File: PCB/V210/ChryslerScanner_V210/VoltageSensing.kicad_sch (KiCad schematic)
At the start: 9 parts

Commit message: Completed schematic.
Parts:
- gave numbers to parts that had none: 9
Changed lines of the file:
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@@
   (symbol (lib_id "Device:R") (at 179.07 99.06 0) (unit 1)
     (in_bom yes) (on_board yes) (fields_autoplaced)
-    (property "Reference" "R?" (id 0) (at 181.61 97.7899 0)
+    (property "Reference" "R28" (id 0) (at 181.61 97.7899 0)
       (effects (font (size 1.27 1.27)) (justify left))
     )
@@
   (symbol (lib_id "power:+12V") (at 95.25 77.47 0) (unit 1)
     (in_bom yes) (on_board yes) (fields_autoplaced)
-    (property "Reference" "#PWR?" (id 0) (at 95.25 81.28 0)
+    (property "Reference" "#PWR035" (id 0) (at 95.25 81.28 0)
       (effects (font (size 1.27 1.27)) hide)
     )
@@
   (symbol (lib_id "Device:R") (at 95.25 99.06 0) (unit 1)
     (in_bom yes) (on_board yes) (fields_autoplaced)
-    (property "Reference" "R?" (id 0) (at 97.79 97.7899 0)
+    (property "Reference" "R24" (id 0) (at 97.79 97.7899 0)
       (effects (font (size 1.27 1.27)) (justify left))
     )
@@
   (symbol (lib_id "Device:R") (at 137.16 86.36 0) (unit 1)
     (in_bom yes) (on_board yes) (fields_autoplaced)
-    (property "Reference" "R?" (id 0) (at 139.7 85.0899 0)
+    (property "Reference" "R25" (id 0) (at 139.7 85.0899 0)
       (effects (font (size 1.27 1.27)) (justify left))
     )
@@
   (symbol (lib_id "power:VAA") (at 137.16 77.47 0) (unit 1)
     (in_bom yes) (on_board yes) (fields_autoplaced)
-    (property "Reference" "#PWR?" (id 0) (at 137.16 81.28 0)
+    (property "Reference" "#PWR037" (id 0) (at 137.16 81.28 0)
       (effects (font (size 1.27 1.27)) hide)
     )
@@
   (symbol (lib_id "Device:R") (at 179.07 86.36 0) (unit 1)
     (in_bom yes) (on_board yes) (fields_autoplaced)
-    (property "Reference" "R?" (id 0) (at 181.61 85.0899 0)
+    (property "Reference" "R27" (id 0) (at 181.61 85.0899 0)
       (effects (font (size 1.27 1.27)) (justify left))
     )
@@
   (symbol (lib_id "power:GND") (at 137.16 109.22 0) (unit 1)
     (in_bom yes) (on_board yes) (fields_autoplaced)
-    (property "Reference" "#PWR?" (id 0) (at 137.16 115.57 0)
+    (property "Reference" "#PWR038" (id 0) (at 137.16 115.57 0)
       (effects (font (size 1.27 1.27)) hide)
     )
@@
   (symbol (lib_id "Device:R") (at 95.25 86.36 0) (unit 1)
     (in_bom yes) (on_board yes) (fields_autoplaced)
-    (property "Reference" "R?" (id 0) (at 97.79 85.0899 0)
+    (property "Reference" "R23" (id 0) (at 97.79 85.0899 0)
       (effects (font (size 1.27 1.27)) (justify left))
     )
@@
   (symbol (lib_id "power:GND") (at 179.07 109.22 0) (unit 1)
     (in_bom yes) (on_board yes) (fields_autoplaced)
-    (property "Reference" "#PWR?" (id 0) (at 179.07 115.57 0)
+    (property "Reference" "#PWR040" (id 0) (at 179.07 115.57 0)
       (effects (font (size 1.27 1.27)) hide)
     )
@@
   (symbol (lib_id "Device:R") (at 137.16 99.06 0) (unit 1)
     (in_bom yes) (on_board yes) (fields_autoplaced)
-    (property "Reference" "R?" (id 0) (at 139.7 97.7899 0)
+    (property "Reference" "R26" (id 0) (at 139.7 97.7899 0)
       (effects (font (size 1.27 1.27)) (justify left))
     )
@@
   (symbol (lib_id "power:GND") (at 95.25 109.22 0) (unit 1)
     (in_bom yes) (on_board yes) (fields_autoplaced)
-    (property "Reference" "#PWR?" (id 0) (at 95.25 115.57 0)
+    (property "Reference" "#PWR036" (id 0) (at 95.25 115.57 0)
       (effects (font (size 1.27 1.27)) hide)
     )
@@
   (symbol (lib_id "Device:C") (at 107.95 99.06 0) (unit 1)
     (in_bom yes) (on_board yes) (fields_autoplaced)
-    (property "Reference" "C?" (id 0) (at 111.76 97.7899 0)
+    (property "Reference" "C16" (id 0) (at 111.76 97.7899 0)
       (effects (font (size 1.27 1.27)) (justify left))
     )
@@
   (symbol (lib_id "Device:C") (at 191.77 99.06 0) (unit 1)
     (in_bom yes) (on_board yes) (fields_autoplaced)
-    (property "Reference" "C?" (id 0) (at 195.58 97.7899 0)
+    (property "Reference" "C18" (id 0) (at 195.58 97.7899 0)
       (effects (font (size 1.27 1.27)) (justify left))
     )
@@
   (symbol (lib_id "power:VPP") (at 179.07 77.47 0) (unit 1)
     (in_bom yes) (on_board yes) (fields_autoplaced)
-    (property "Reference" "#PWR?" (id 0) (at 179.07 81.28 0)
+    (property "Reference" "#PWR039" (id 0) (at 179.07 81.28 0)
       (effects (font (size 1.27 1.27)) hide)
     )
@@
   (symbol (lib_id "Device:C") (at 149.86 99.06 0) (unit 1)
     (in_bom yes) (on_board yes) (fields_autoplaced)
-    (property "Reference" "C?" (id 0) (at 153.67 97.7899 0)
-      (effects (font (size 1.27 1.27)) (justify left))
-    )
+    (property "Reference" "C17" (id 0) (at 153.67 97.7899 0)
+      (effects (font (size 1.27 1.27)) (justify left))
+    )

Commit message: WIP
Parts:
- C16, C17, C18: footprint (none) -> Capacitor_SMD:C_0603_1608Metric
- R21: renamed from R23; footprint (none) -> Resistor_SMD:R_0603_1608Metric
- R22: renamed from R24; footprint (none) -> Resistor_SMD:R_0603_1608Metric
- R23: renamed from R25; footprint (none) -> Resistor_SMD:R_0603_1608Metric
- R24: renamed from R26; footprint (none) -> Resistor_SMD:R_0603_1608Metric
- R25: renamed from R27; footprint (none) -> Resistor_SMD:R_0603_1608Metric
- R26: renamed from R28; footprint (none) -> Resistor_SMD:R_0603_1608Metric
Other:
- title: Chrysler Scanner -> TJ Diag
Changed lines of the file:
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@@
   (paper "A4")
   (title_block
-    (title "Chrysler Scanner")
-    (date "2023-06-25")
-    (rev "V2.11")
+    (title "TJ Diag")
+    (date "2023-07-01")
+    (rev "V1.00")
     (company "andy@britishideas.com")
     (comment 1 "V210/ChryslerScanner_V210/schematic/ChryslerScanner_V210_schematic.pdf")
@@
   (symbol (lib_id "Device:R") (at 179.07 99.06 0) (unit 1)
     (in_bom yes) (on_board yes) (fields_autoplaced)
-    (property "Reference" "R28" (id 0) (at 181.61 97.7899 0)
+    (property "Reference" "R26" (id 0) (at 181.61 97.7899 0)
       (effects (font (size 1.27 1.27)) (justify left))
     )
@@
       (effects (font (size 1.27 1.27)) (justify left))
     )
-    (property "Footprint" "" (id 2) (at 177.292 99.06 90)
+    (property "Footprint" "Resistor_SMD:R_0603_1608Metric" (id 2) (at 177.292 99.06 90)
       (effects (font (size 1.27 1.27)) hide)
     )
@@
   (symbol (lib_id "power:+12V") (at 95.25 77.47 0) (unit 1)
     (in_bom yes) (on_board yes) (fields_autoplaced)
-    (property "Reference" "#PWR035" (id 0) (at 95.25 81.28 0)
+    (property "Reference" "#PWR031" (id 0) (at 95.25 81.28 0)
       (effects (font (size 1.27 1.27)) hide)
     )
@@
   (symbol (lib_id "Device:R") (at 95.25 99.06 0) (unit 1)
     (in_bom yes) (on_board yes) (fields_autoplaced)
-    (property "Reference" "R24" (id 0) (at 97.79 97.7899 0)
+    (property "Reference" "R22" (id 0) (at 97.79 97.7899 0)
       (effects (font (size 1.27 1.27)) (justify left))
     )
@@
       (effects (font (size 1.27 1.27)) (justify left))
     )
-    (property "Footprint" "" (id 2) (at 93.472 99.06 90)
+    (property "Footprint" "Resistor_SMD:R_0603_1608Metric" (id 2) (at 93.472 99.06 90)
       (effects (font (size 1.27 1.27)) hide)
     )
@@
   (symbol (lib_id "Device:R") (at 137.16 86.36 0) (unit 1)
     (in_bom yes) (on_board yes) (fields_autoplaced)
-    (property "Reference" "R25" (id 0) (at 139.7 85.0899 0)
+    (property "Reference" "R23" (id 0) (at 139.7 85.0899 0)
       (effects (font (size 1.27 1.27)) (justify left))
     )
@@
       (effects (font (size 1.27 1.27)) (justify left))
     )
-    (property "Footprint" "" (id 2) (at 135.382 86.36 90)
+    (property "Footprint" "Resistor_SMD:R_0603_1608Metric" (id 2) (at 135.382 86.36 90)
       (effects (font (size 1.27 1.27)) hide)
     )
@@
   (symbol (lib_id "power:VAA") (at 137.16 77.47 0) (unit 1)
     (in_bom yes) (on_board yes) (fields_autoplaced)
-    (property "Reference" "#PWR037" (id 0) (at 137.16 81.28 0)
+    (property "Reference" "#PWR033" (id 0) (at 137.16 81.28 0)
       (effects (font (size 1.27 1.27)) hide)
     )
@@
   (symbol (lib_id "Device:R") (at 179.07 86.36 0) (unit 1)
     (in_bom yes) (on_board yes) (fields_autoplaced)
-    (property "Reference" "R27" (id 0) (at 181.61 85.0899 0)
+    (property "Reference" "R25" (id 0) (at 181.61 85.0899 0)
       (effects (font (size 1.27 1.27)) (justify left))
     )
@@
       (effects (font (size 1.27 1.27)) (justify left))
     )
-    (property "Footprint" "" (id 2) (at 177.292 86.36 90)
+    (property "Footprint" "Resistor_SMD:R_0603_1608Metric" (id 2) (at 177.292 86.36 90)
       (effects (font (size 1.27 1.27)) hide)
     )
@@
   (symbol (lib_id "power:GND") (at 137.16 109.22 0) (unit 1)
     (in_bom yes) (on_board yes) (fields_autoplaced)
-    (property "Reference" "#PWR038" (id 0) (at 137.16 115.57 0)
+    (property "Reference" "#PWR034" (id 0) (at 137.16 115.57 0)
       (effects (font (size 1.27 1.27)) hide)
     )
@@
   (symbol (lib_id "Device:R") (at 95.25 86.36 0) (unit 1)
     (in_bom yes) (on_board yes) (fields_autoplaced)
-    (property "Reference" "R23" (id 0) (at 97.79 85.0899 0)
+    (property "Reference" "R21" (id 0) (at 97.79 85.0899 0)
       (effects (font (size 1.27 1.27)) (justify left))
     )
@@
       (effects (font (size 1.27 1.27)) (justify left))
     )
-    (property "Footprint" "" (id 2) (at 93.472 86.36 90)
+    (property "Footprint" "Resistor_SMD:R_0603_1608Metric" (id 2) (at 93.472 86.36 90)
       (effects (font (size 1.27 1.27)) hide)
     )
@@
   (symbol (lib_id "power:GND") (at 179.07 109.22 0) (unit 1)
     (in_bom yes) (on_board yes) (fields_autoplaced)
-    (property "Reference" "#PWR040" (id 0) (at 179.07 115.57 0)
+    (property "Reference" "#PWR036" (id 0) (at 179.07 115.57 0)
       (effects (font (size 1.27 1.27)) hide)
     )
@@
   (symbol (lib_id "Device:R") (at 137.16 99.06 0) (unit 1)
     (in_bom yes) (on_board yes) (fields_autoplaced)
-    (property "Reference" "R26" (id 0) (at 139.7 97.7899 0)
+    (property "Reference" "R24" (id 0) (at 139.7 97.7899 0)
       (effects (font (size 1.27 1.27)) (justify left))
     )
@@
       (effects (font (size 1.27 1.27)) (justify left))
     )
-    (property "Footprint" "" (id 2) (at 135.382 99.06 90)
+    (property "Footprint" "Resistor_SMD:R_0603_1608Metric" (id 2) (at 135.382 99.06 90)
       (effects (font (size 1.27 1.27)) hide)
     )
@@
   (symbol (lib_id "power:GND") (at 95.25 109.22 0) (unit 1)
     (in_bom yes) (on_board yes) (fields_autoplaced)
-    (property "Reference" "#PWR036" (id 0) (at 95.25 115.57 0)
+    (property "Reference" "#PWR032" (id 0) (at 95.25 115.57 0)
       (effects (font (size 1.27 1.27)) hide)
     )
@@
       (effects (font (size 1.27 1.27)) (justify left))
     )
-    (property "Footprint" "" (id 2) (at 108.9152 102.87 0)
+    (property "Footprint" "Capacitor_SMD:C_0603_1608Metric" (id 2) (at 108.9152 102.87 0)
       (effects (font (size 1.27 1.27)) hide)
     )
@@
       (effects (font (size 1.27 1.27)) (justify left))
     )
-    (property "Footprint" "" (id 2) (at 192.7352 102.87 0)
+    (property "Footprint" "Capacitor_SMD:C_0603_1608Metric" (id 2) (at 192.7352 102.87 0)
       (effects (font (size 1.27 1.27)) hide)
     )
@@
   (symbol (lib_id "power:VPP") (at 179.07 77.47 0) (unit 1)
     (in_bom yes) (on_board yes) (fields_autoplaced)
-    (property "Reference" "#PWR039" (id 0) (at 179.07 81.28 0)
+    (property "Reference" "#PWR035" (id 0) (at 179.07 81.28 0)
       (effects (font (size 1.27 1.27)) hide)
     )
@@
       (effects (font (size 1.27 1.27)) (justify left))
     )
-    (property "Footprint" "" (id 2) (at 150.8252 102.87 0)
-      (effects (font (size 1.27 1.27)) hide)
-    )
+    (property "Footprint" "Capacitor_SMD:C_0603_1608Metric" (id 2) (at 150.8252 102.87 0)
+      (effects (font (size 1.27 1.27)) hide)
+    )

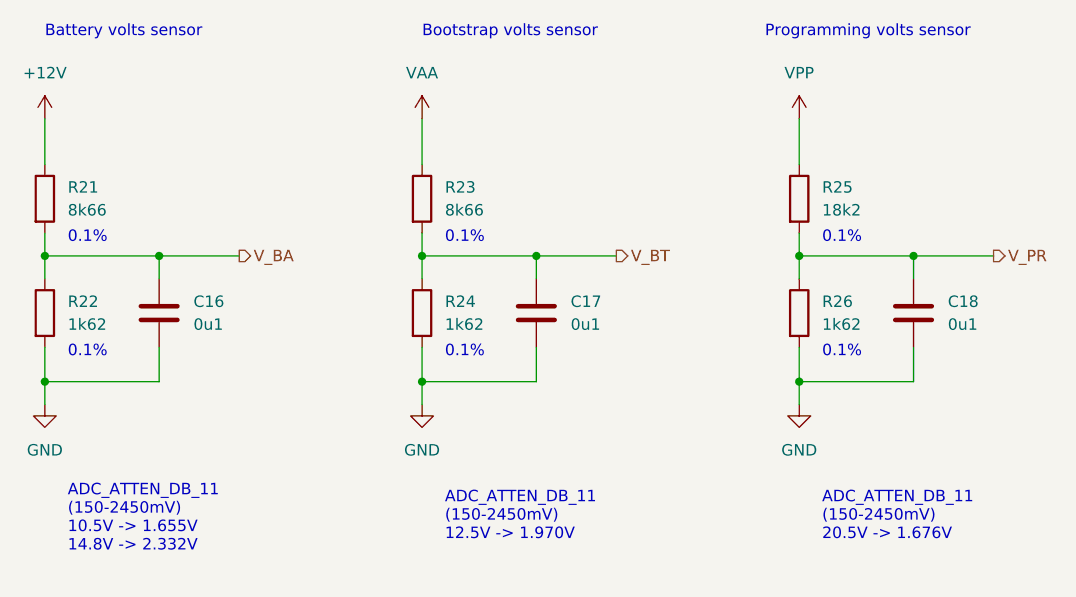
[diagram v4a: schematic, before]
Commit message: Added CCD back in - needed for early TJs.
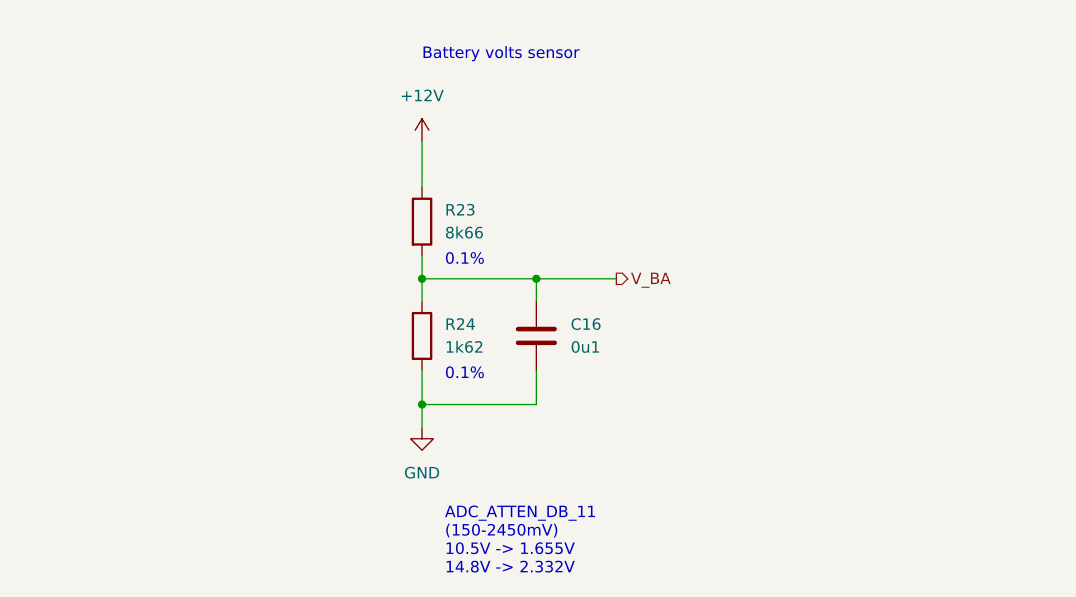
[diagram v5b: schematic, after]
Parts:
- removed C17, C18: 0u1, Capacitor_SMD:C_0603_1608Metric, symbol Device:C
- removed R23: 8k66, Resistor_SMD:R_0603_1608Metric, symbol Device:R
- removed R24, R26: 1k62, Resistor_SMD:R_0603_1608Metric, symbol Device:R
- removed R25: 18k2, Resistor_SMD:R_0603_1608Metric, symbol Device:R
- renumbered R21 to R23, R22 to R24
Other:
- note removed: "ADC_ATTEN_DB_11 (150-2450mV) 12.5V -> 1.970V"
- note removed: "ADC_ATTEN_DB_11 (150-2450mV) 20.5V -> 1.676V"
- note removed: "Bootstrap volts sensor"
- note removed: "Programming volts sensor"
- moved on the sheet: C16, R23, R24
